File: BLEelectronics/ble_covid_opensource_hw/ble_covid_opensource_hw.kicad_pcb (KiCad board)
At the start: 2 copper layers, 34.3 x 28.3 mm, 75 parts, among them IC1 LTC4412xS6, IC2 LTC4054LES5-4.2#TRPBF, IC3 PCF8523T, IC4 MX25R6435FM2IL0, J1 USB_B_Micro, J3 Conn_02x05_Odd_Even, Q1 Si2307CDS, SW1 NO, SW2 SW_MEC_5G, U1 BAT-HLD-001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

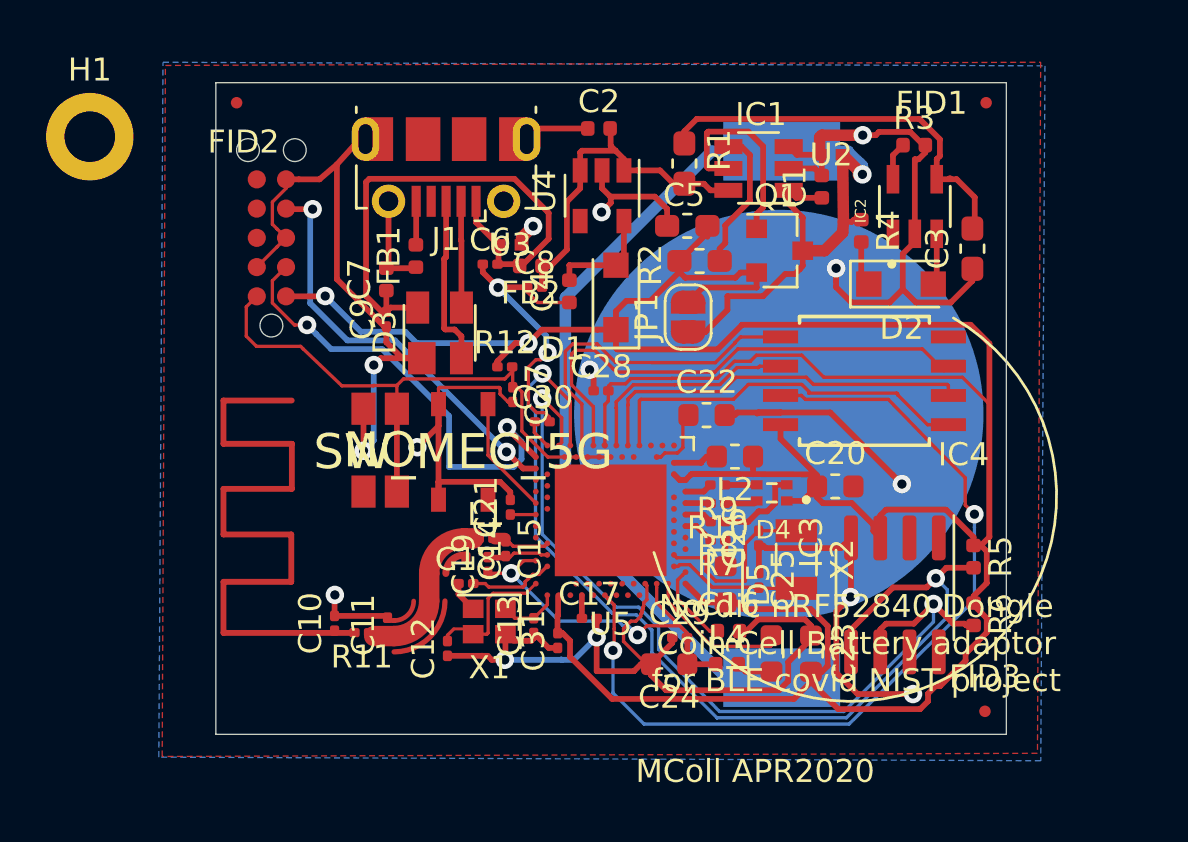
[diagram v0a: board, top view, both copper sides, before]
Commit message: Moved power from pin 3 VBat to pin 8 Vdd on RTC. Swapped SIO3 and SDA on 1a and 1b. Changed battery footprint to allow backside routing for Flash and USB data. Todo: Unbreak MVP1B layout rerouting.
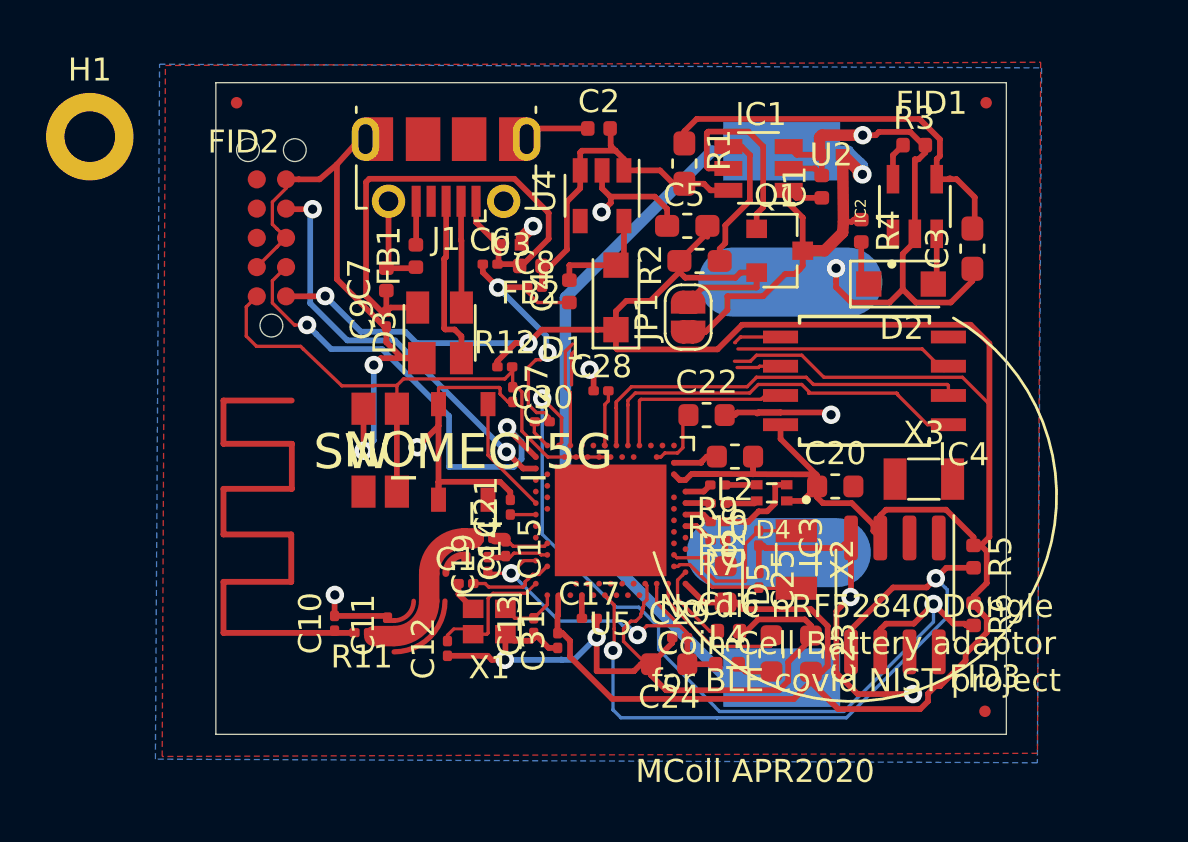
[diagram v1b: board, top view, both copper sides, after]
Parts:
- added X3: 32.768KHZ, Crystal:Crystal_SMD_3215-2Pin_3.2x1.5mm, F.Cu at (157.4, 89.9)
- U1: footprint 0my_footprints:BAT-HLD-001 -> 0my_footprints:BAT-HLD-001_smallerGND
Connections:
- IC3 pad 3: /VDD_3V -> Net-(IC3-Pad3)
- IC3 pad 8: Net-(IC3-Pad8) -> /VDD_3V
- U5 pad A14: /SIO3 -> /SDA
- U5 pad AD10: /SO -> /CS
- U5 pad AD12: /SCLK -> /SO
- U5 pad AD16: /WP -> /SCLK
- U5 pad AD18: /SI -> /WP
- U5 pad AD20: /SDA -> /SI
- U5 pad AD4: /nRF52840_QIAA_R/D- -> /D-
- U5 pad AD6: /nRF52840_QIAA_R/D+ -> /D+
- U5 pad AD8: /CS -> /SIO3
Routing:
- net /SIO3: track 37.9 -> 8.16 mm, vias 2 -> 0
- net /SDA: track 43.9 -> 30.9 mm
- net /WP: track 21.8 -> 11.1 mm
- net /SI: track 14.7 -> 6.73 mm
- net /SCLK: track 9.71 -> 1.91 mm
- net /VDD_3V: track 148.3 -> 142.2 mm
- net GND: track 163.1 -> 158.8 mm
- net /SO: track 17.1 -> 19.3 mm
- net /CS: track 16.5 -> 17.0 mm
